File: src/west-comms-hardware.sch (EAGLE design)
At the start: 9 parts, among them X1 PC104_STANDARD1

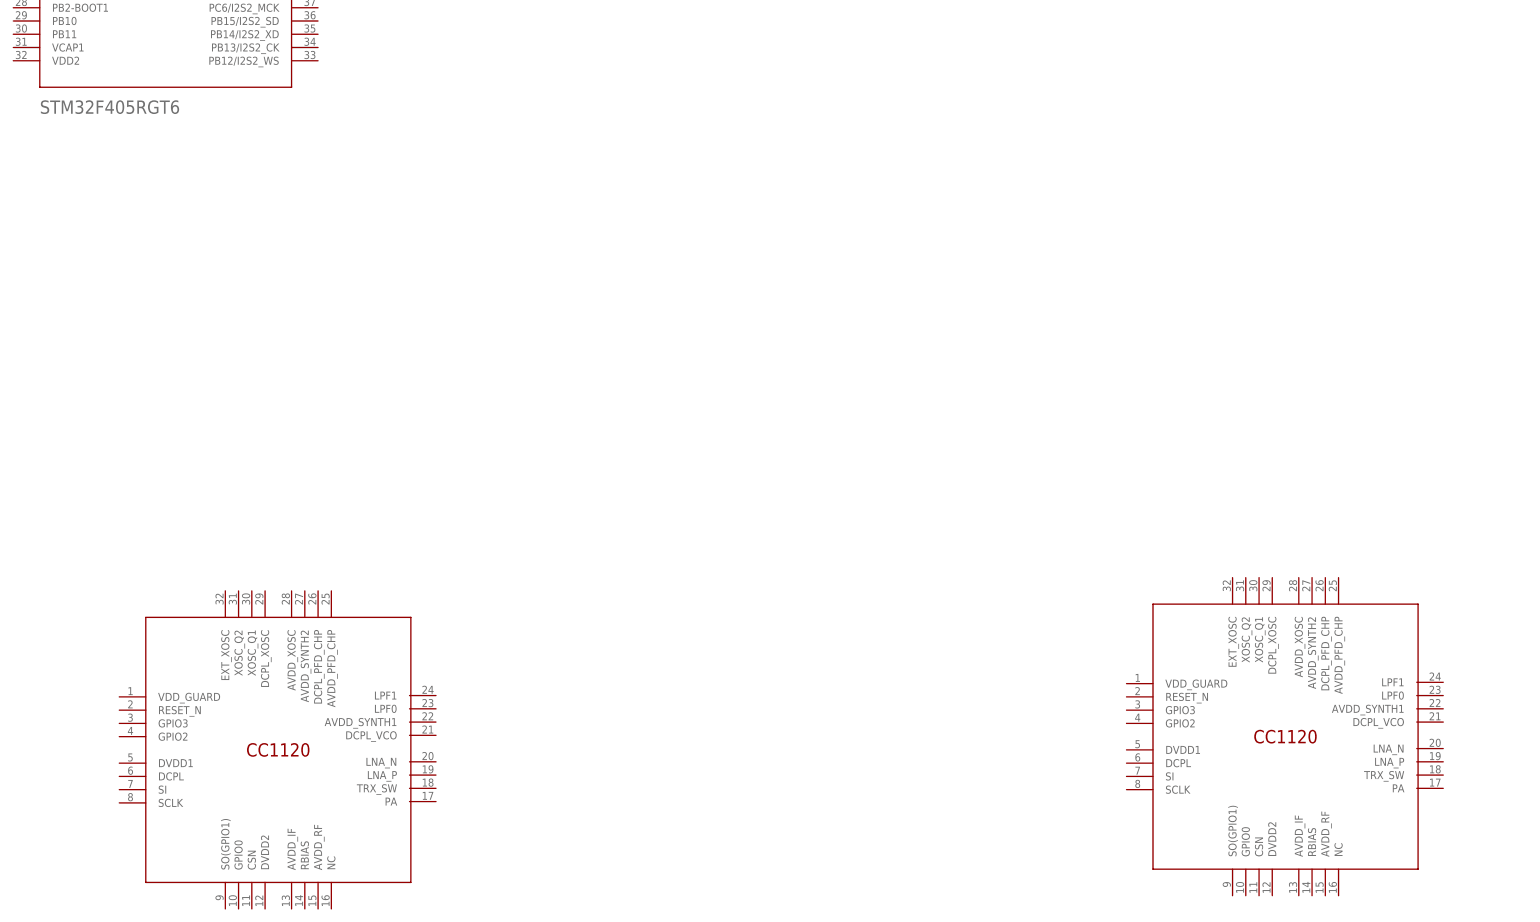
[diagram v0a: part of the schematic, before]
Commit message: Adjust CAN net
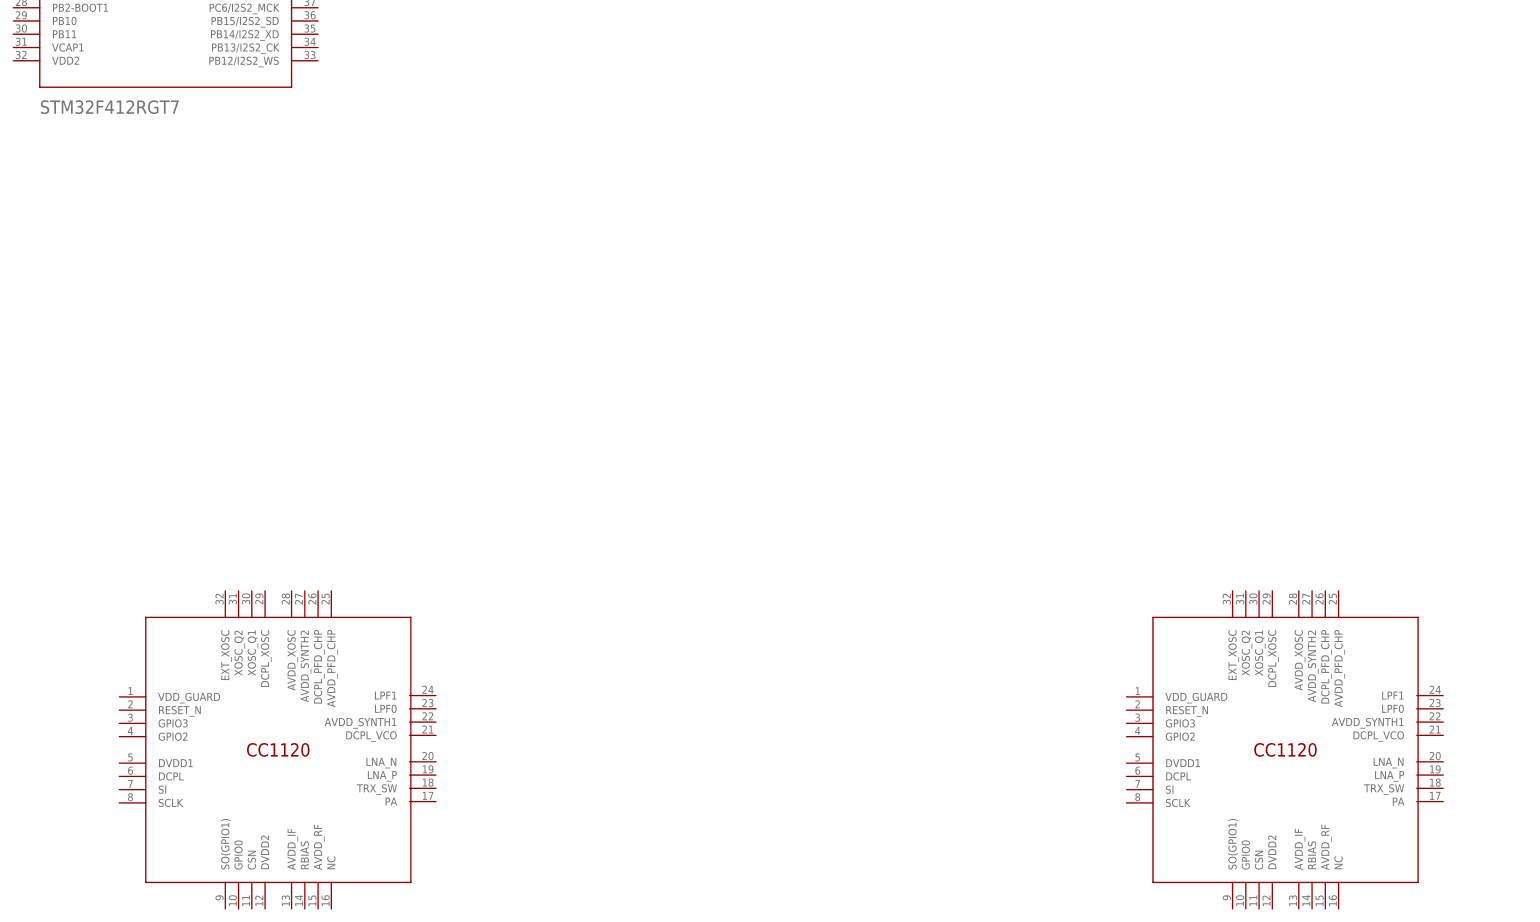
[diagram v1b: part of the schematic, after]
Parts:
- U$1: value STM32F405RGT6 -> STM32F412RGT7
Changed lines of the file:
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@@
 <parts>
 <part name="X1" library="con-pc104" library_urn="urn:adsk.eagle:library:171" deviceset="PC104_STANDARD" device="1" package3d_urn="urn:adsk.eagle:package:9297/1"/>
-<part name="U$1" library="SparkFun-IC-Microcontroller" library_urn="urn:adsk.eagle:library:525" deviceset="STM32F405RG" device="" package3d_urn="urn:adsk.eagle:package:38936/1" value="STM32F405RGT6"/>
+<part name="U$1" library="SparkFun-IC-Microcontroller" library_urn="urn:adsk.eagle:library:525" deviceset="STM32F405RG" device="" package3d_urn="urn:adsk.eagle:package:38936/1" value="STM32F412RGT7"/>
 <part name="U$2" library="west-eagle-library" deviceset="CC1120" device=""/>
 <part name="U$3" library="west-eagle-library" deviceset="CC1120" device=""/>
@@
 </instance>
 <instance part="U$2" gate="G$1" x="121.92" y="177.8" smashed="yes"/>
-<instance part="U$3" gate="G$1" x="314.96" y="180.34" smashed="yes"/>
+<instance part="U$3" gate="G$1" x="314.96" y="177.8" smashed="yes"/>
 <instance part="FRAME1" gate="G$1" x="0" y="0" smashed="yes"/>
 <instance part="FRAME1" gate="G$2" x="452.12" y="0" smashed="yes">
